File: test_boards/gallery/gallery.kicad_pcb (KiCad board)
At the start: 2 copper layers, 25 parts

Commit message: tweaking caps
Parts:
- added C***: Val**, ELCAP_10_20_V, F.Cu at (69.8, 25.4)
- added C***: Val**, ELCAP_20_52_V, F.Cu at (80.0, 26.7)
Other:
- board text added: "capacitors_PL"
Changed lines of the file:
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@@
     (area 17.142178 16.28 401.217201 279.357448)
     (thickness 1.6)
-    (drawings 8)
+    (drawings 9)
     (tracks 22)
     (zones 0)
-    (modules 25)
+    (modules 27)
     (nets 1)
   )
@@
     )
   )
+  (module ELCAP_10_20_V (layer F.Cu)
+    (at 69.85 25.4)
+    (descr "Electrolytic Capacitor, vertical, 0.1\" pins, 0.2\" body")
+    (tags CP)
+    (fp_text reference C*** (at 1.27 -1.397) (layer F.SilkS)
+      (effects (font (size 0.635 0.635) (thickness 0.127)))
+    )
+    (fp_text value Val** (at 1.27 1.524) (layer F.SilkS)
+      (effects (font (size 0.635 0.635) (thickness 0.127)))
+    )
+    (fp_circle (center 1.27 0) (end 3.81 0) (layer F.SilkS) (width 0.3048))
+    (pad 1 thru_hole rect (at 0 0) (size 2.2479 1.4986) (drill 0.8128 (offset -0.37465 0))
+      (layers *.Cu *.Mask F.SilkS)
+    )
+    (pad 2 thru_hole oval (at 2.54 0) (size 2.2479 1.4986) (drill 0.8128 (offset 0.37465 0))
+      (layers *.Cu *.Mask F.SilkS)
+    )
+    (model discret/c_vert_c2v10.wrl
+      (at (xyz 0 0 0))
+      (scale (xyz 1 1 1))
+      (rotate (xyz 0 0 0))
+    )
+  )
+  (module ELCAP_20_52_V (layer F.Cu)
+    (at 80.01 26.67)
+    (descr "Electrolytic Capacitor, vertical, 0.2\" pins, 0.52\" body")
+    (tags CP)
+    (fp_text reference C*** (at 2.54 -2.54) (layer F.SilkS)
+      (effects (font (size 1.016 1.016) (thickness 0.2032)))
+    )
+    (fp_text value Val** (at 2.54 2.54) (layer F.SilkS)
+      (effects (font (size 1.016 1.016) (thickness 0.2032)))
+    )
+    (fp_circle (center 2.54 0) (end 9.144 0) (layer F.SilkS) (width 0.3048))
+    (pad 1 thru_hole rect (at 0 0) (size 2.6289 1.7526) (drill 1.016 (offset -0.43815 0))
+      (layers *.Cu *.Mask F.SilkS)
+    )
+    (pad 2 thru_hole oval (at 5.08 0) (size 2.6289 1.7526) (drill 1.016 (offset 0.43815 0))
+      (layers *.Cu *.Mask F.SilkS)
+    )
+    (model discret/c_vert_c2v10.wrl
+      (at (xyz 0 0 0))
+      (scale (xyz 1 1 1))
+      (rotate (xyz 0 0 0))
+    )
+  )
+  (gr_text capacitors_PL (at 68.58 17.78) (layer F.SilkS)
+    (effects (font (size 1.5 1.5) (thickness 0.3)) (justify left))
+  )
   (gr_text connectors_PL (at 17.78 140.97) (layer F.SilkS)

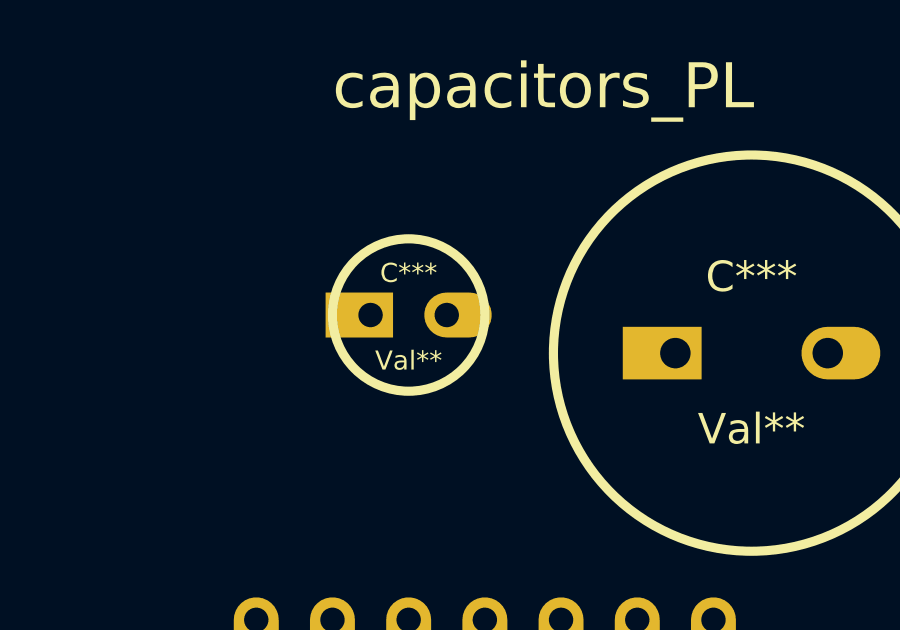
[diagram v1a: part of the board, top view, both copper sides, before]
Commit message: adding polarity to caps
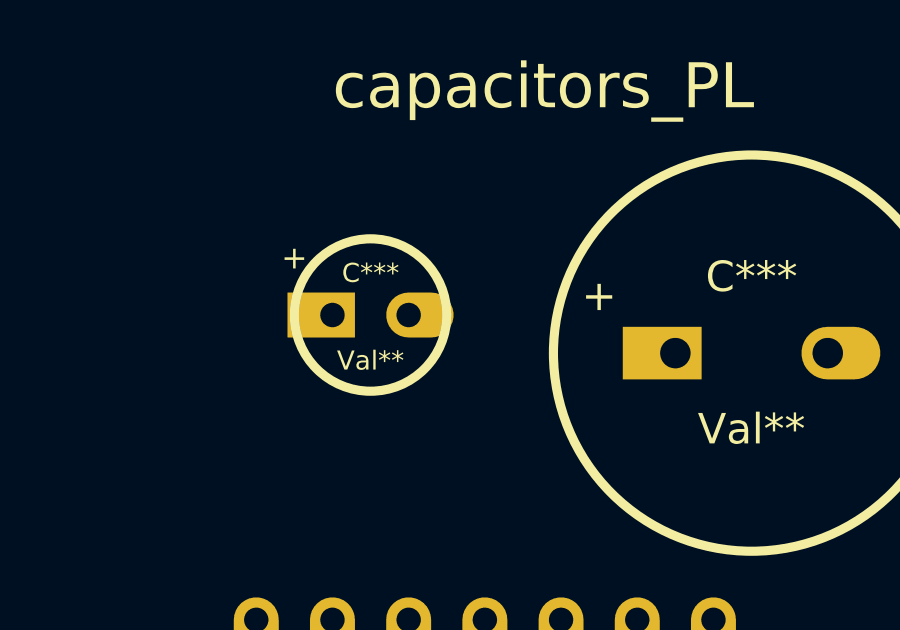
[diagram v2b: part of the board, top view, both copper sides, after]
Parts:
- moved C*** 1.27 mm to (68.6, 25.4)
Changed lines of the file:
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@@
   )
   (module ELCAP_10_20_V (layer F.Cu)
-    (at 69.85 25.4)
+    (at 68.58 25.4)
     (descr "Electrolytic Capacitor, vertical, 0.1\" pins, 0.2\" body")
     (tags CP)
@@
     (fp_text value Val** (at 1.27 1.524) (layer F.SilkS)
       (effects (font (size 0.635 0.635) (thickness 0.127)))
+    )
+    (fp_text user + (at -1.27 -1.905) (layer F.SilkS)
+      (effects (font (size 0.762 0.762) (thickness 0.1524)))
     )
     (fp_circle (center 1.27 0) (end 3.81 0) (layer F.SilkS) (width 0.3048))
@@
       (effects (font (size 1.016 1.016) (thickness 0.2032)))
     )
+    (fp_text user + (at -2.54 -1.905) (layer F.SilkS)
+      (effects (font (size 1.016 1.016) (thickness 0.2032)))
+    )

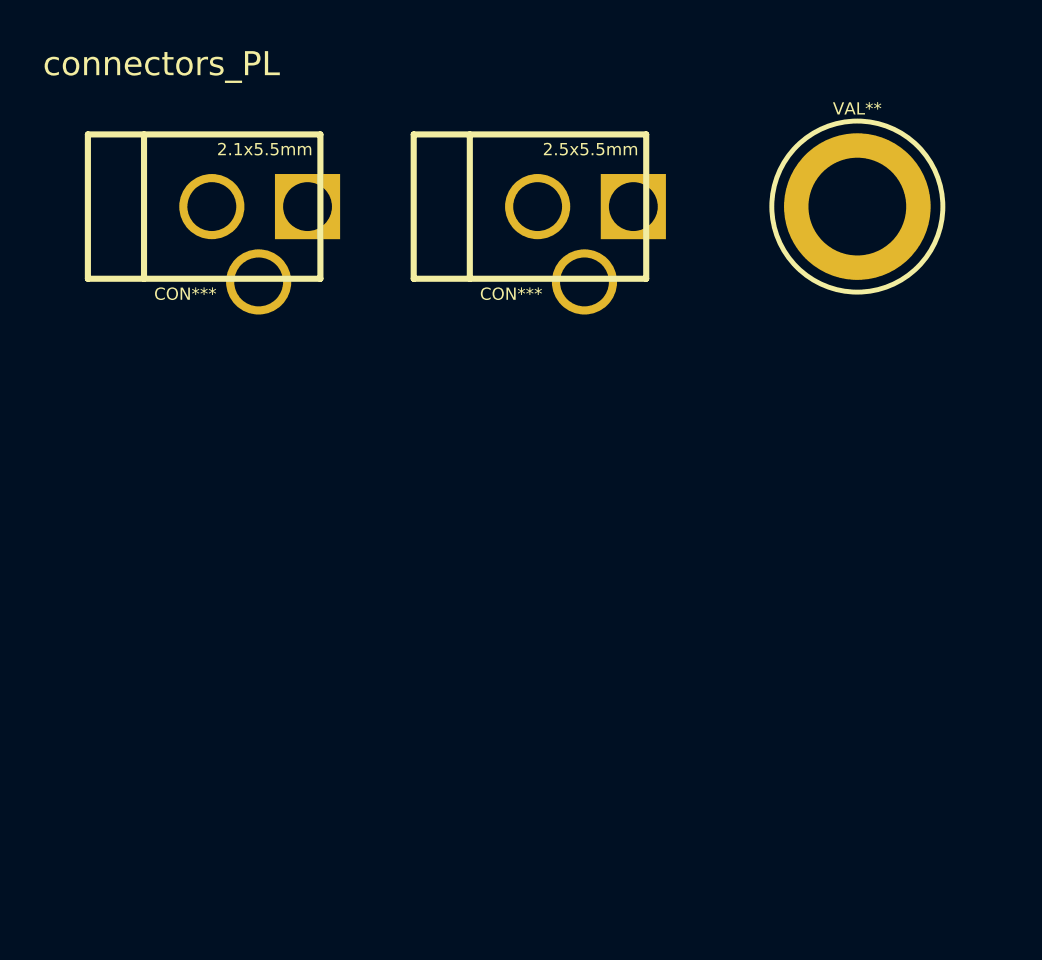
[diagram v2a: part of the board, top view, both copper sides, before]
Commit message: updating connectors and swithes footprints
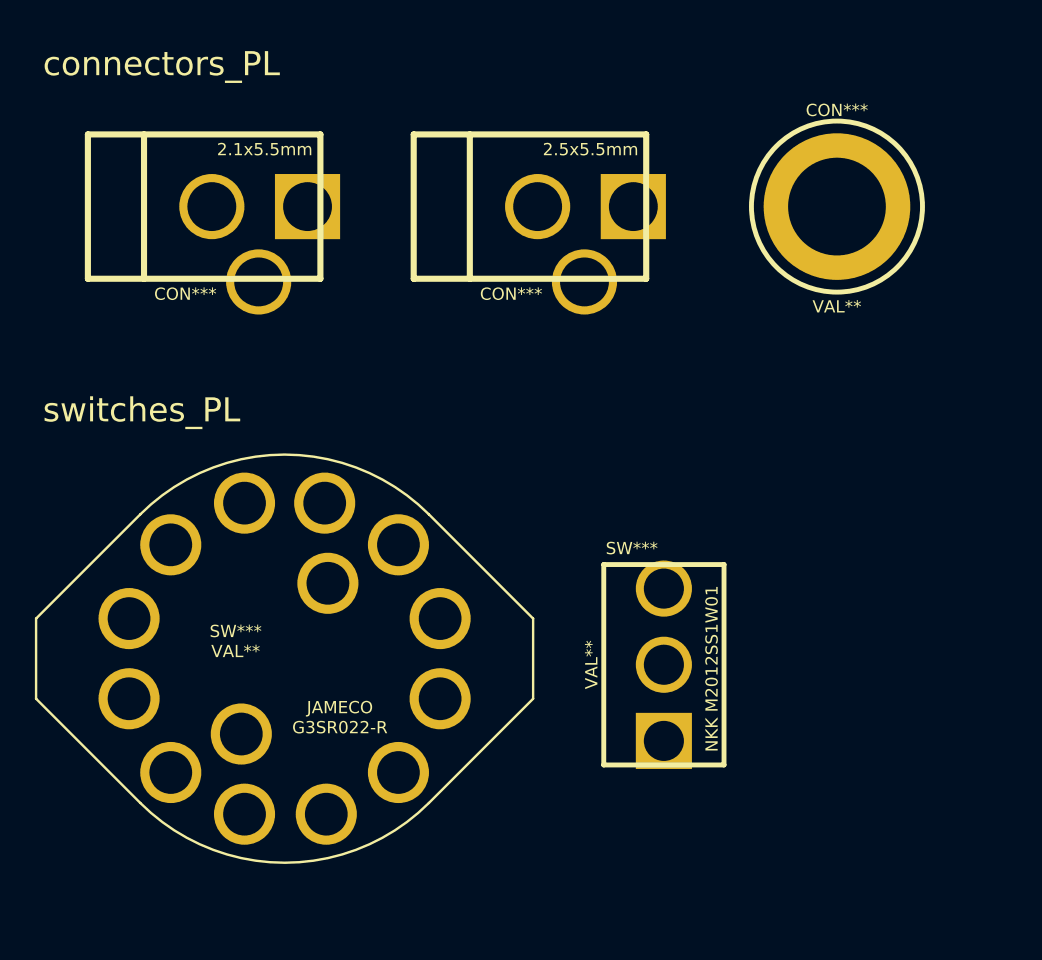
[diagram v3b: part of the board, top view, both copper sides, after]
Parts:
- removed Banana_A: VAL**, Banana_A
- added CON***: VAL**, Banana_A, F.Cu at (67.3, 149.9)
- added SW***: VAL**, M2012SS1W01, F.Cu at (56.5, 178.4)
- added SW***: VAL**, G3SR022-R, F.Cu at (35.6, 173.4)
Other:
- board text added: "switches_PL"
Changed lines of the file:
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@@
     (area 17.142178 16.28 401.217201 279.357448)
     (thickness 1.6)
-    (drawings 9)
+    (drawings 10)
     (tracks 22)
     (zones 0)
-    (modules 27)
+    (modules 29)
     (nets 1)
   )
@@
     )
   )
-  (module Banana_A (layer F.Cu)
-    (at 68.58 149.86)
-    (fp_text reference Banana_A (at 0 6.096) (layer F.SilkS) hide
-      (effects (font (size 0.762 0.762) (thickness 0.1524)))
-    )
-    (fp_text value VAL** (at 0 -6.096) (layer F.SilkS)
-      (effects (font (size 0.762 0.762) (thickness 0.1524)))
-    )
-    (fp_circle (center 0 0) (end 5.334 0) (layer F.SilkS) (width 0.3048))
-    (pad 1 thru_hole circle (at 0 0) (size 9.144 9.144) (drill 6.096)
-      (layers *.Cu *.Mask F.SilkS)
-    )
-  )
   (module R_AXIAL_0W25 (layer F.Cu)
     (at 20.32 25.4)
@@
     )
   )
+  (module M2012SS1W01 (layer F.Cu)
+    (at 56.515 178.435)
+    (descr "NKK Mini SPDT toggle switch (on-on)")
+    (fp_text reference SW*** (at -2 -7.25) (layer F.SilkS)
+      (effects (font (size 0.762 0.762) (thickness 0.1524)))
+    )
+    (fp_text value VAL** (at -4.5 0 90) (layer F.SilkS)
+      (effects (font (size 0.762 0.762) (thickness 0.1524)))
+    )
+    (fp_text user "NKK M2012SS1W01" (at 3 0.25 90) (layer F.SilkS)
+      (effects (font (size 0.762 0.762) (thickness 0.1524)))
+    )
+    (fp_line (start -3.75 6.25) (end -3.75 -6.25) (layer F.SilkS) (width 0.3048))
+    (fp_line (start -3.75 -6.25) (end 3.75 -6.25) (layer F.SilkS) (width 0.3048))
+    (fp_line (start 3.75 -6.25) (end 3.75 6.25) (layer F.SilkS) (width 0.3048))
+    (fp_line (start 3.75 6.25) (end -3.75 6.25) (layer F.SilkS) (width 0.3048))
+    (pad 1 thru_hole rect (at 0 4.75) (size 3.5 3.5) (drill 2.5)
+      (layers *.Cu *.Mask F.SilkS)
+    )
+    (pad 2 thru_hole circle (at 0 0) (size 3.5 3.5) (drill 2.5)
+      (layers *.Cu *.Mask F.SilkS)
+    )
+    (pad 3 thru_hole circle (at 0 -4.75) (size 3.5 3.5) (drill 2.5)
+      (layers *.Cu *.Mask F.SilkS)
+    )
+  )
+  (module G3SR022-R (layer F.Cu)
+    (at 35.56 173.355)
+    (fp_text reference SW*** (at -5.75 3) (layer F.SilkS)
+      (effects (font (size 0.762 0.762) (thickness 0.1524)))
+    )
+    (fp_text value VAL** (at -5.75 4.25) (layer F.SilkS)
+      (effects (font (size 0.762 0.762) (thickness 0.1524)))
+    )
+    (fp_text user JAMECO (at 0.75 7.75) (layer F.SilkS)
+      (effects (font (size 0.762 0.762) (thickness 0.1524)))
+    )
+    (fp_text user G3SR022-R (at 0.75 9) (layer F.SilkS)
+      (effects (font (size 0.762 0.762) (thickness 0.1524)))
+    )
+    (fp_line (start 6.3 13.7) (end 12.8 7.2) (layer F.SilkS) (width 0.15))
+    (fp_line (start 6.3 -4.3) (end 12.8 2.2) (layer F.SilkS) (width 0.15))
+    (fp_line (start -11.7 13.7) (end -18.2 7.2) (layer F.SilkS) (width 0.15))
+    (fp_line (start -18.2 2.2) (end -11.7 -4.3) (layer F.SilkS) (width 0.15))
+    (fp_arc (start -2.7 4.7) (end 6.3 13.7) (angle 90) (layer F.SilkS) (width 0.15))
+    (fp_arc (start -2.7 4.7) (end -11.7 -4.3) (angle 90) (layer F.SilkS) (width 0.15))
+    (fp_line (start -18.2 2.2) (end -18.2 7.2) (layer F.SilkS) (width 0.15))
+    (fp_line (start 12.8 2.2) (end 12.8 7.2) (layer F.SilkS) (width 0.15))
+    (pad 13 thru_hole circle (at -12.4 7.2) (size 3.81 3.81) (drill 2.667)
+      (layers *.Cu *.Mask F.SilkS)
+    )
+    (pad 11 thru_hole circle (at -5.2 14.4) (size 3.81 3.81) (drill 2.667)
+      (layers *.Cu *.Mask F.SilkS)
+    )
+    (pad 12 thru_hole circle (at -9.8 11.8) (size 3.81 3.81) (drill 2.667)
+      (layers *.Cu *.Mask F.SilkS)
+    )
+    (pad 10 thru_hole circle (at -0.1 14.4) (size 3.81 3.81) (drill 2.667)
+      (layers *.Cu *.Mask F.SilkS)
+    )
+    (pad 4 thru_hole circle (at -0.2 -5) (size 3.81 3.81) (drill 2.667)
+      (layers *.Cu *.Mask F.SilkS)
+    )
+    (pad 3 thru_hole circle (at -5.2 -5) (size 3.81 3.81) (drill 2.667)
+      (layers *.Cu *.Mask F.SilkS)
+    )
+    (pad 14 thru_hole circle (at -12.4 2.2) (size 3.81 3.81) (drill 2.667)
+      (layers *.Cu *.Mask F.SilkS)
+    )
+    (pad 6 thru_hole circle (at 7 2.2) (size 3.81 3.81) (drill 2.667)
+      (layers *.Cu *.Mask F.SilkS)
+    )
+    (pad 7 thru_hole circle (at 7 7.2) (size 3.81 3.81) (drill 2.667)
+      (layers *.Cu *.Mask F.SilkS)
+    )
+    (pad 2 thru_hole circle (at -9.8 -2.4) (size 3.81 3.81) (drill 2.667)
+      (layers *.Cu *.Mask F.SilkS)
+    )
+    (pad 5 thru_hole circle (at 4.4 -2.4) (size 3.81 3.81) (drill 2.667)
+      (layers *.Cu *.Mask F.SilkS)
+    )
+    (pad 9 thru_hole circle (at 4.4 11.8) (size 3.81 3.81) (drill 2.667)
+      (layers *.Cu *.Mask F.SilkS)
+    )
+    (pad 1 thru_hole circle (at 0 0) (size 3.81 3.81) (drill 2.667)
+      (layers *.Cu *.Mask F.SilkS)
+    )
+    (pad 8 thru_hole circle (at -5.4 9.4) (size 3.81 3.81) (drill 2.667)
+      (layers *.Cu *.Mask F.SilkS)
+    )
+  )
+  (module Banana_A (layer F.Cu)
+    (at 67.31 149.86)
+    (fp_text reference CON*** (at 0 -6) (layer F.SilkS)
+      (effects (font (size 0.762 0.762) (thickness 0.1524)))
+    )
+    (fp_text value VAL** (at 0 6.25) (layer F.SilkS)
+      (effects (font (size 0.762 0.762) (thickness 0.1524)))
+    )
+    (fp_circle (center 0 0) (end 5.334 0) (layer F.SilkS) (width 0.3048))
+    (pad 1 thru_hole circle (at 0 0) (size 9.144 9.144) (drill 6.096)
+      (layers *.Cu *.Mask F.SilkS)
+    )
+  )
+  (gr_text switches_PL (at 17.78 162.56) (layer F.SilkS)
+    (effects (font (size 1.5 1.5) (thickness 0.3)) (justify left))
+  )
   (gr_text capacitors_PL (at 68.58 17.78) (layer F.SilkS)

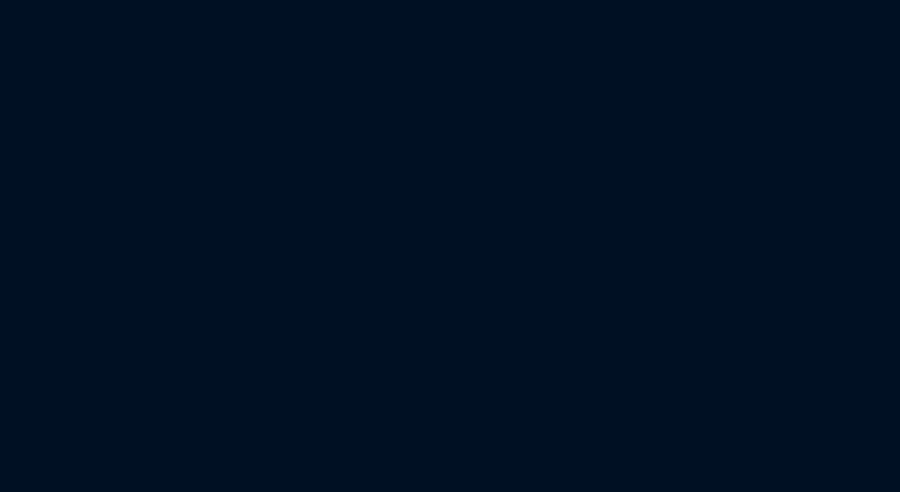
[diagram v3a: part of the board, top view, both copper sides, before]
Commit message: adding diodes
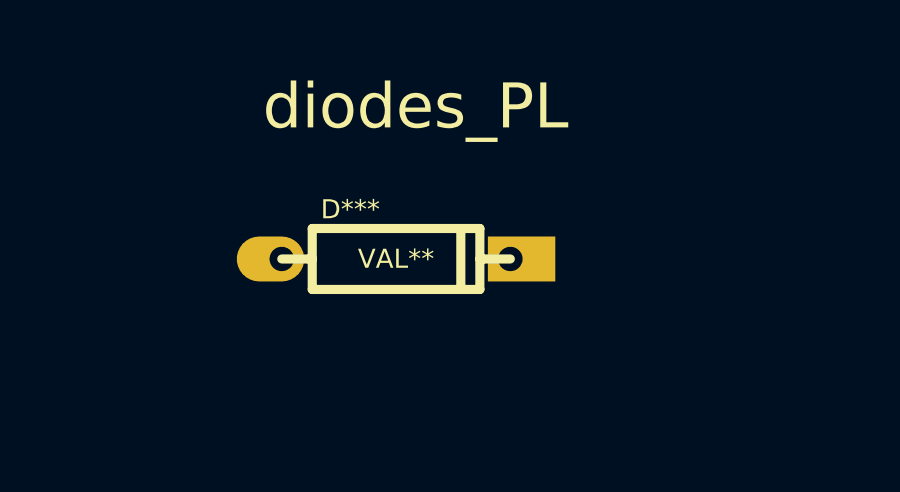
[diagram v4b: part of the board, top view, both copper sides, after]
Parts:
- added D***: VAL**, DIODE_3, F.Cu at (116.8, 22.9)
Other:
- board text added: "diodes_PL"
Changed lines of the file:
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@@
     (links 0)
     (no_connects 0)
-    (area 17.142178 16.28 401.217201 279.357448)
+    (area 17.030999 16.28 401.217201 279.357448)
     (thickness 1.6)
-    (drawings 10)
+    (drawings 11)
     (tracks 22)
     (zones 0)
-    (modules 29)
+    (modules 30)
     (nets 1)
   )
@@
     (mod_text_size 1 1)
     (mod_text_width 0.15)
-    (pad_size 2.6289 1.7526)
-    (pad_drill 1.016)
+    (pad_size 2.2479 1.4986)
+    (pad_drill 0.8128)
     (pad_to_mask_clearance 0)
     (aux_axis_origin 0 0)
@@
     )
   )
+  (module DIODE_3 (layer F.Cu)
+    (at 116.84 22.86)
+    (descr "Diode, 0.3\"")
+    (tags "DIODE DEV")
+    (fp_text reference D*** (at 2.286 -1.651) (layer F.SilkS)
+      (effects (font (size 0.635 0.635) (thickness 0.127)))
+    )
+    (fp_text value VAL** (at 3.81 0) (layer F.SilkS)
+      (effects (font (size 0.635 0.635) (thickness 0.127)))
+    )
+    (fp_line (start 1.016 0) (end 0 0) (layer F.SilkS) (width 0.3048))
+    (fp_line (start 6.604 0) (end 7.62 0) (layer F.SilkS) (width 0.3048))
+    (fp_line (start 1.016 1.016) (end 6.604 1.016) (layer F.SilkS) (width 0.3048))
+    (fp_line (start 6.604 -1.016) (end 1.016 -1.016) (layer F.SilkS) (width 0.3048))
+    (fp_line (start 5.969 -1.016) (end 5.969 1.016) (layer F.SilkS) (width 0.3048))
+    (fp_line (start 6.604 0) (end 6.604 -1.016) (layer F.SilkS) (width 0.3048))
+    (fp_line (start 1.016 -1.016) (end 1.016 0) (layer F.SilkS) (width 0.3048))
+    (fp_line (start 1.016 0) (end 1.016 1.016) (layer F.SilkS) (width 0.3048))
+    (fp_line (start 6.604 1.016) (end 6.604 0) (layer F.SilkS) (width 0.3048))
+    (pad 2 thru_hole rect (at 7.62 0) (size 2.2479 1.4986) (drill 0.8128 (offset 0.37465 0))
+      (layers *.Cu *.Mask F.SilkS)
+    )
+    (pad 1 thru_hole oval (at 0 0) (size 2.2479 1.4986) (drill 0.8128 (offset -0.37465 0))
+      (layers *.Cu *.Mask F.SilkS)
+    )
+    (model discret/diode.wrl
+      (at (xyz 0 0 0))
+      (scale (xyz 0.3 0.3 0.3))
+      (rotate (xyz 0 0 0))
+    )
+  )
+  (gr_text diodes_PL (at 116.205 17.78) (layer F.SilkS)
+    (effects (font (size 1.5 1.5) (thickness 0.3)) (justify left))
+  )
   (gr_text switches_PL (at 17.78 162.56) (layer F.SilkS)
